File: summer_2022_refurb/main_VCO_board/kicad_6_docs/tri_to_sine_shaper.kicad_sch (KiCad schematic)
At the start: 15 parts

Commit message: Main VCO progress
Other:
- title: (none) -> Josh Ox Ribon Synth Main VCO board
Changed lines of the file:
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@@
 (kicad_sch (version 20211123) (generator eeschema)
   (paper "A4")
+  (title_block
+    (title "Josh Ox Ribon Synth Main VCO board")
+    (date "2022-06-18")
+    (rev "0")
+    (comment 2 "creativecommons.org/licences/by/4.0")
+    (comment 3 "license: CC by 4.0")
+    (comment 4 "Author: Jordan Acete")
+  )
   (junction (at 207.01 72.39) (diameter 0) (color 0 0 0 0)
   )

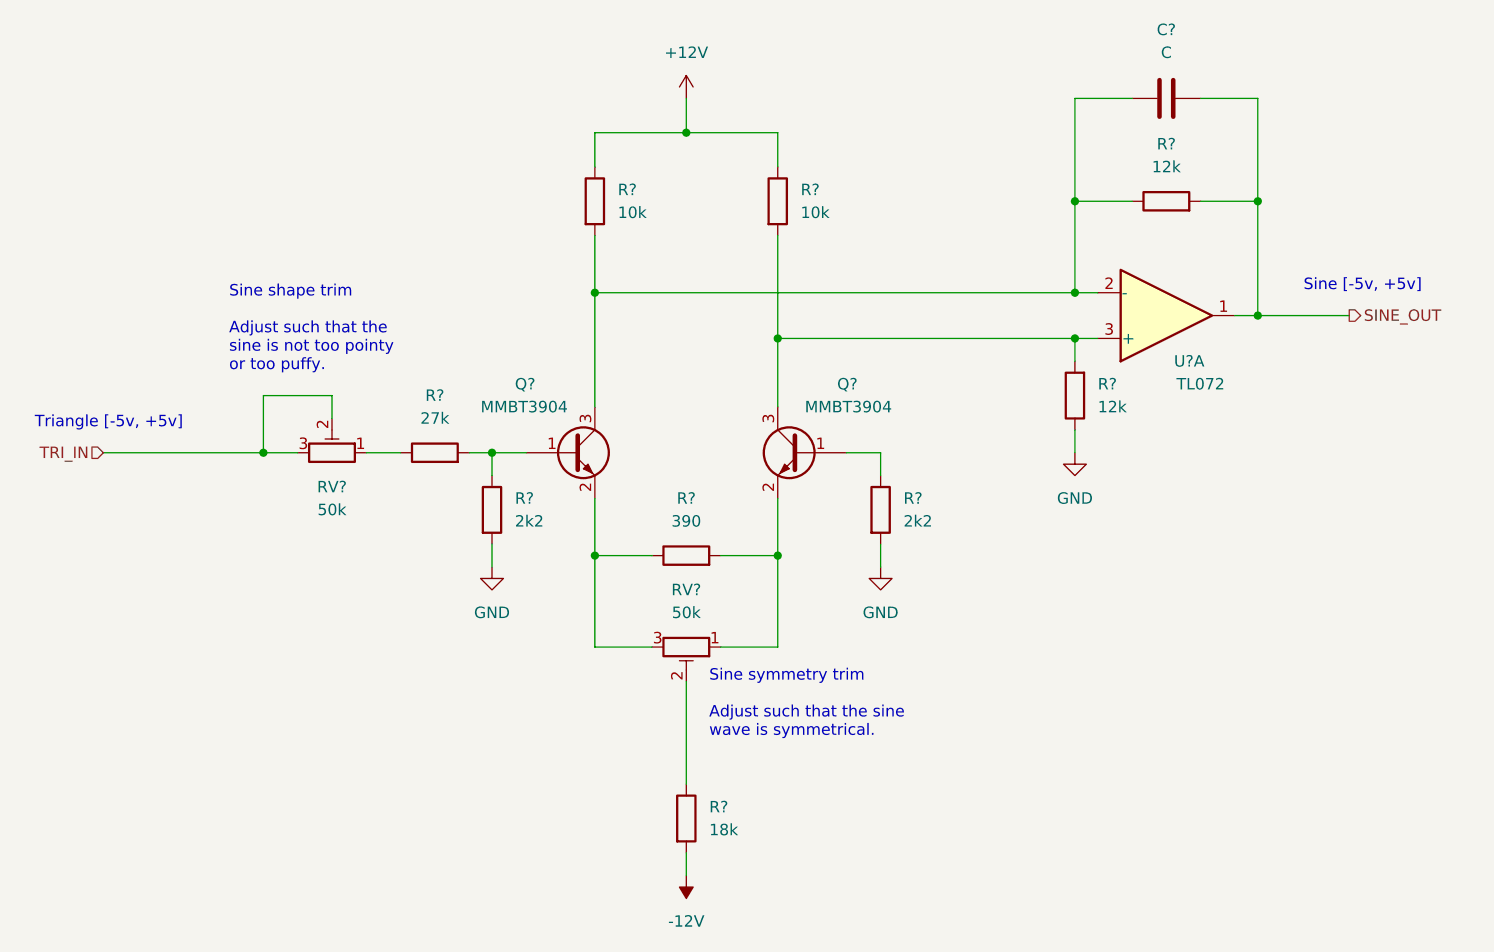
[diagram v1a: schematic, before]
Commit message: Progress on main VCO, schem getting close but not done
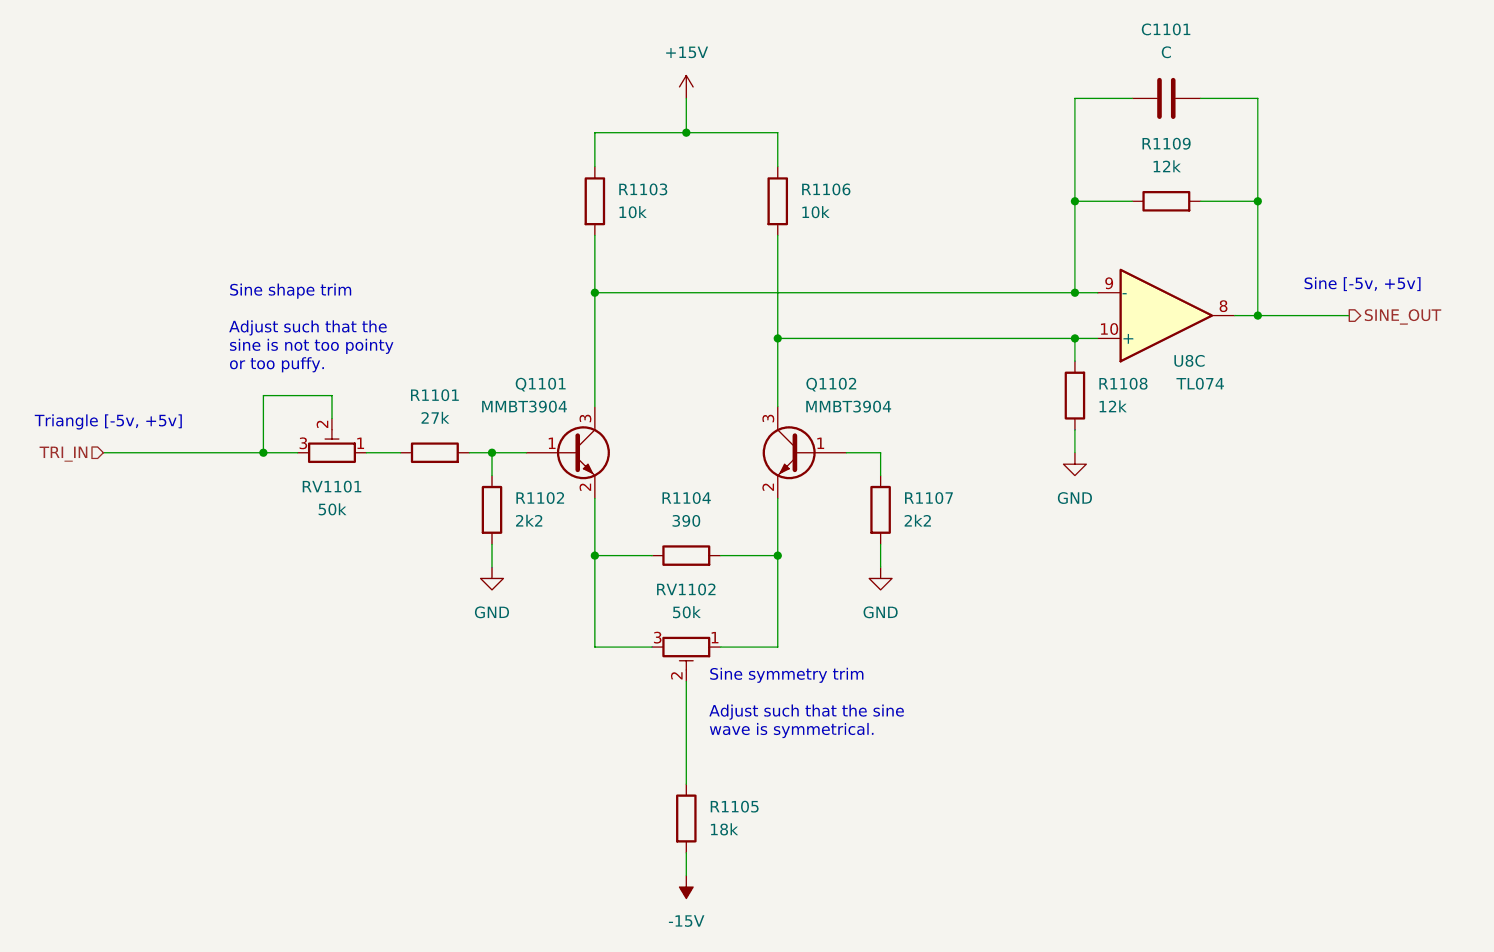
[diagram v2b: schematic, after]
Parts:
- removed U?: TL072, symbol Amplifier_Operational:TL072
- added U8: TL074, symbol Amplifier_Operational:TL074
- gave numbers to parts that had none: 14
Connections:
- net SINE_OUT: now also U8.8
- net at C1101.1, Q1101.3 (C), R1103.2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: now also U8.9 (-)
- net at Q1102.3 (C), R1106.2, R1108.2: now also U8.10 (+)
- net +12V renamed +15V
- net -12V renamed -15V

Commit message: Main VCO rough parts placement
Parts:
- C1101: footprint (none) -> Capacitor_SMD:C_0805_2012Metric
- R1101, R1102, R1103, R1104, R1105, R1106, R1107, R1108, R1109: footprint (none) -> Resistor_SMD:R_0805_2012Metric
- RV1101, RV1102: footprint (none) -> Potentiometer_THT:Potentiometer_Bourns_3296W_Vertical
- U8: footprint (none) -> Package_SO:SOIC-14_3.9x8.7mm_P1.27mm
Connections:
- net SINE_OUT: now also U8.1; no longer U8.8
- net at C1101.1, Q1101.3 (C), R1103.2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: now also U8.2 (-); no longer U8.9 (-)
- net at Q1102.3 (C), R1106.2, R1108.2: now also U8.3 (+); no longer U8.10 (+)
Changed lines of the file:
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@@
       (effects (font (size 1.27 1.27)) (justify left))
     )
-    (property "Footprint" "" (id 2) (at 131.572 72.39 90)
+    (property "Footprint" "Resistor_SMD:R_0805_2012Metric" (id 2) (at 131.572 72.39 90)
       (effects (font (size 1.27 1.27)) hide)
     )
@@
       (effects (font (size 1.27 1.27)) (justify left))
     )
-    (property "Footprint" "" (id 2) (at 141.732 140.97 90)
+    (property "Footprint" "Resistor_SMD:R_0805_2012Metric" (id 2) (at 141.732 140.97 90)
       (effects (font (size 1.27 1.27)) hide)
     )
@@
     (property "Reference" "RV1101" (id 0) (at 104.14 104.14 90))
     (property "Value" "50k" (id 1) (at 104.14 106.68 90))
-    (property "Footprint" "" (id 2) (at 104.14 100.33 0)
+    (property "Footprint" "Potentiometer_THT:Potentiometer_Bourns_3296W_Vertical" (id 2) (at 104.14 100.33 0)
       (effects (font (size 1.27 1.27)) hide)
     )
@@
       (effects (font (size 1.27 1.27)) (justify left))
     )
-    (property "Footprint" "" (id 2) (at 151.892 72.39 90)
+    (property "Footprint" "Resistor_SMD:R_0805_2012Metric" (id 2) (at 151.892 72.39 90)
       (effects (font (size 1.27 1.27)) hide)
     )
@@
       (effects (font (size 1.27 1.27)) (justify left))
     )
-    (property "Footprint" "" (id 2) (at 163.322 106.68 90)
+    (property "Footprint" "Resistor_SMD:R_0805_2012Metric" (id 2) (at 163.322 106.68 90)
       (effects (font (size 1.27 1.27)) hide)
     )
@@
     (property "Reference" "R1101" (id 0) (at 115.57 93.98 90))
     (property "Value" "27k" (id 1) (at 115.57 96.52 90))
-    (property "Footprint" "" (id 2) (at 115.57 102.108 90)
+    (property "Footprint" "Resistor_SMD:R_0805_2012Metric" (id 2) (at 115.57 102.108 90)
       (effects (font (size 1.27 1.27)) hide)
     )
@@
       (effects (font (size 1.27 1.27)) (justify right))
     )
-    (property "Footprint" "" (id 2) (at 188.468 93.98 90)
+    (property "Footprint" "Resistor_SMD:R_0805_2012Metric" (id 2) (at 188.468 93.98 90)
       (effects (font (size 1.27 1.27)) hide)
     )
@@
       (effects (font (size 1.27 1.27)) (justify left))
     )
-    (property "Footprint" "" (id 2) (at 120.142 106.68 90)
+    (property "Footprint" "Resistor_SMD:R_0805_2012Metric" (id 2) (at 120.142 106.68 90)
       (effects (font (size 1.27 1.27)) hide)
     )
@@
     (property "Reference" "R1104" (id 0) (at 143.51 105.41 90))
     (property "Value" "390" (id 1) (at 143.51 107.95 90))
-    (property "Footprint" "" (id 2) (at 143.51 113.538 90)
+    (property "Footprint" "Resistor_SMD:R_0805_2012Metric" (id 2) (at 143.51 113.538 90)
       (effects (font (size 1.27 1.27)) hide)
     )
@@
     (property "Reference" "R1109" (id 0) (at 196.85 66.04 90))
     (property "Value" "12k" (id 1) (at 196.85 68.58 90))
-    (property "Footprint" "" (id 2) (at 196.85 74.168 90)
+    (property "Footprint" "Resistor_SMD:R_0805_2012Metric" (id 2) (at 196.85 74.168 90)
       (effects (font (size 1.27 1.27)) hide)
     )
@@
     (property "Reference" "C1101" (id 0) (at 196.85 53.34 90))
     (property "Value" "C" (id 1) (at 196.85 55.88 90))
-    (property "Footprint" "" (id 2) (at 200.66 59.9948 0)
+    (property "Footprint" "Capacitor_SMD:C_0805_2012Metric" (id 2) (at 200.66 59.9948 0)
       (effects (font (size 1.27 1.27)) hide)
     )
@@
     (property "Reference" "RV1102" (id 0) (at 143.51 115.57 90))
     (property "Value" "50k" (id 1) (at 143.51 118.11 90))
-    (property "Footprint" "" (id 2) (at 143.51 121.92 0)
+    (property "Footprint" "Potentiometer_THT:Potentiometer_Bourns_3296W_Vertical" (id 2) (at 143.51 121.92 0)
       (effects (font (size 1.27 1.27)) hide)
     )
@@
     (pin "1")
   )
-  (symbol (lib_id "Amplifier_Operational:TL074") (at 196.85 85.09 0) (mirror x) (unit 3)
+  (symbol (lib_id "Amplifier_Operational:TL074") (at 196.85 85.09 0) (mirror x) (unit 1)
     (in_bom yes) (on_board yes)
     (property "Reference" "U8" (id 0) (at 199.39 90.17 0))
     (property "Value" "TL074" (id 1) (at 200.66 92.71 0))
-    (property "Footprint" "" (id 2) (at 195.58 87.63 0)
-      (effects (font (size 1.27 1.27)) hide)
-    )
+    (property "Footprint" "Package_SO:SOIC-14_3.9x8.7mm_P1.27mm" (id 2) (at 195.58 87.63 0)
+      (effects (font (size 1.27 1.27)) hide)
+    )
